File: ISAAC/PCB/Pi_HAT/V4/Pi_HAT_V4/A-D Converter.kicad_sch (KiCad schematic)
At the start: 1 part, among them U2 MCP3008-I/SL

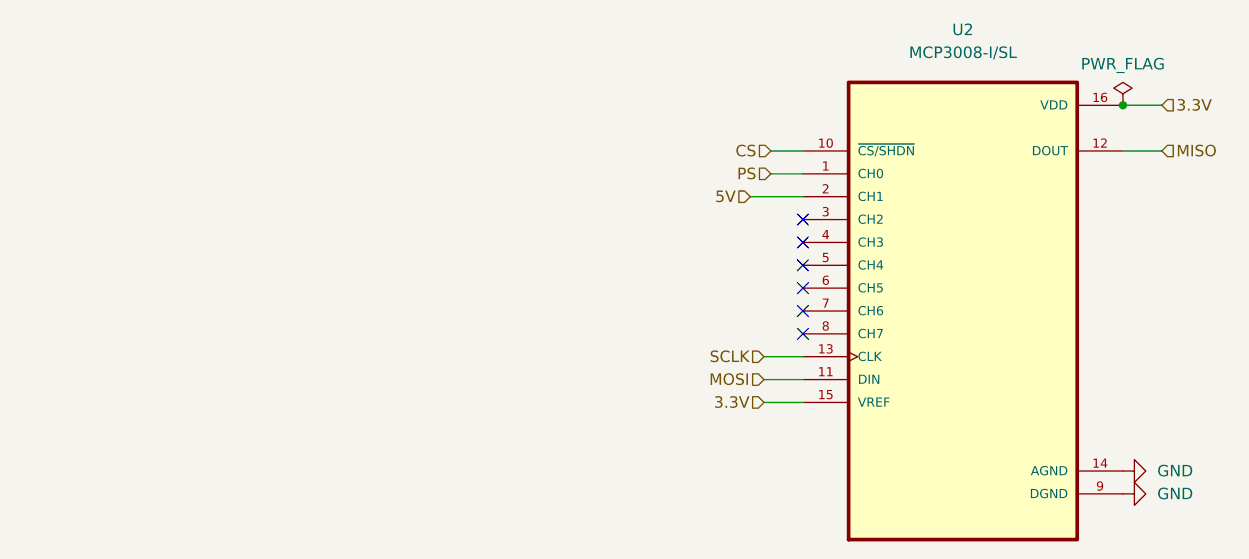
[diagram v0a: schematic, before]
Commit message: Updated
Started SPARK grant and updated controller and PCB
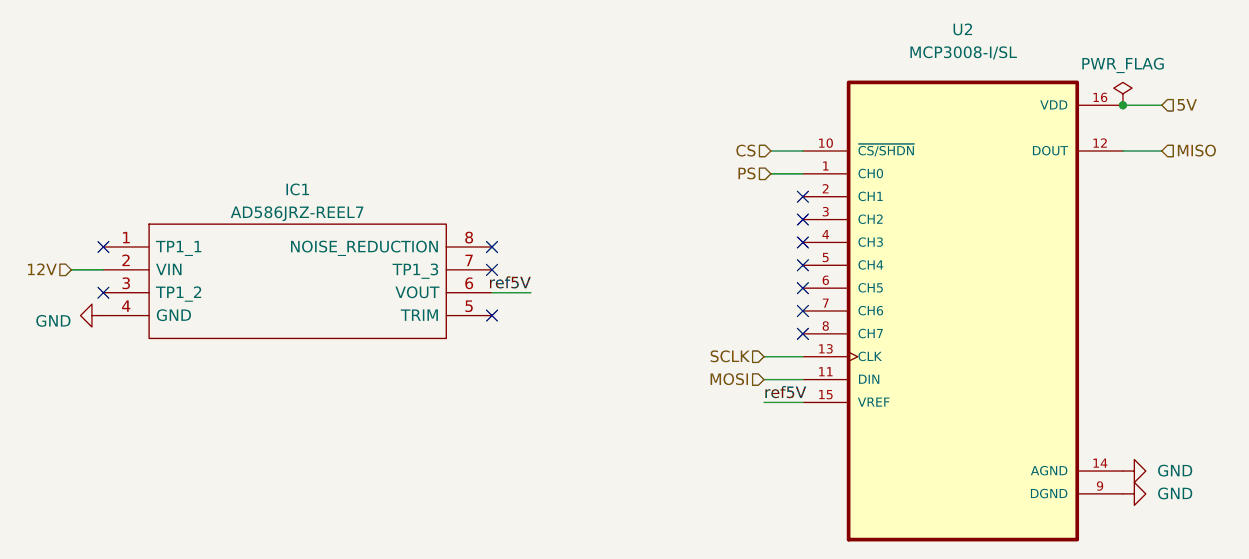
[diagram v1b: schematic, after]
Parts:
- added IC1: AD586JRZ-REEL7, refV:SOIC127P600X175-8N, symbol AD586JRZ-REEL7:AD586JRZ-REEL7
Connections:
- net 5V: now also U2.16 (VDD); no longer U2.2 (CH1)
- net GND: now also IC1.4 (GND)
- net 3.3V renamed ref5V
- net ref5V: now also IC1.6 (VOUT); no longer U2.16 (VDD)
- new net 12V: IC1.2 (VIN)
- no-connect marks 6 -> 12
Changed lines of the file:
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@@
   (junction (at 161.29 68.072) (diameter 0) (color 0 0 0 0)
   )
+  (no_connect (at 48.006 88.9))
+  (no_connect (at 48.006 83.82))
   (no_connect (at 125.73 88.392))
   (no_connect (at 125.73 90.932))
   (no_connect (at 125.73 93.472))
+  (no_connect (at 91.186 86.36))
+  (no_connect (at 125.73 78.232))
   (no_connect (at 125.73 83.312))
   (no_connect (at 125.73 85.852))
   (no_connect (at 125.73 80.772))
-  (wire (pts (xy 119.888 78.232) (xy 125.73 78.232))
-    (stroke (width 0) (type default))
-  )
+  (no_connect (at 91.186 91.44))
+  (no_connect (at 91.186 83.82))
   (wire (pts (xy 161.29 73.152) (xy 165.608 73.152))
     (stroke (width 0) (type default))
@@
     (stroke (width 0) (type default))
   )
+  (wire (pts (xy 44.45 86.36) (xy 48.006 86.36))
+    (stroke (width 0) (type default))
+  )
+  (wire (pts (xy 91.186 88.9) (xy 95.504 88.9))
+    (stroke (width 0) (type default))
+  )
   (wire (pts (xy 121.412 96.012) (xy 125.73 96.012))
     (stroke (width 0) (type default))
@@
     (stroke (width 0) (type default))
   )
-  (hierarchical_label "3.3V" (shape input) (at 121.412 101.092 180) (fields_autoplaced)
-    (effects (font (size 1.27 1.27)) (justify right))
+  (label "ref5V" (at 95.504 88.9 180) (fields_autoplaced)
+    (effects (font (size 1.27 1.27)) (justify right bottom))
   )
-  (hierarchical_label "3.3V" (shape input) (at 165.608 68.072 0) (fields_autoplaced)
-    (effects (font (size 1.27 1.27)) (justify left))
+  (label "ref5V" (at 121.412 101.092 0) (fields_autoplaced)
+    (effects (font (size 1.27 1.27)) (justify left bottom))
   )
   (hierarchical_label "SCLK" (shape input) (at 121.412 96.012 180) (fields_autoplaced)
@@
     (effects (font (size 1.27 1.27)) (justify left))
   )
-  (hierarchical_label "5V" (shape input) (at 119.888 78.232 180) (fields_autoplaced)
+  (hierarchical_label "12V" (shape input) (at 44.45 86.36 180) (fields_autoplaced)
     (effects (font (size 1.27 1.27)) (justify right))
+  )
+  (hierarchical_label "5V" (shape input) (at 165.608 68.072 0) (fields_autoplaced)
+    (effects (font (size 1.27 1.27)) (justify left))
   )
   (hierarchical_label "MOSI" (shape input) (at 121.412 98.552 180) (fields_autoplaced)
@@
   (hierarchical_label "PS" (shape input) (at 122.174 75.692 180) (fields_autoplaced)
     (effects (font (size 1.27 1.27)) (justify right))
+  )
+  (symbol (lib_id "AD586JRZ-REEL7:AD586JRZ-REEL7") (at 48.006 83.82 0) (unit 1)
+    (in_bom yes) (on_board yes) (dnp no) (fields_autoplaced)
+    (property "Reference" "IC1" (at 69.596 77.47 0)
+      (effects (font (size 1.27 1.27)))
+    )
+    (property "Value" "AD586JRZ-REEL7" (at 69.596 80.01 0)
+      (effects (font (size 1.27 1.27)))
+    )
+    (property "Footprint" "refV:SOIC127P600X175-8N" (at 87.376 81.28 0)
+      (effects (font (size 1.27 1.27)) (justify left) hide)
+    )
+    (property "Datasheet" "https://www.analog.com/media/en/technical-documentation/data-sheets/AD586.pdf" (at 87.376 83.82 0)
+      (effects (font (size 1.27 1.27)) (justify left) hide)
+    )
+    (property "Description" "Voltage References IC, MONO HI PREC .5V REF IC" (at 87.376 86.36 0)
+      (effects (font (size 1.27 1.27)) (justify left) hide)
+    )
+    (property "Height" "1.75" (at 87.376 88.9 0)
+      (effects (font (size 1.27 1.27)) (justify left) hide)
+    )
+    (property "Mouser Part Number" "584-AD586JRZ-R7" (at 87.376 91.44 0)
+      (effects (font (size 1.27 1.27)) (justify left) hide)
+    )
+    (property "Mouser Price/Stock" "https://www.mouser.co.uk/ProductDetail/Analog-Devices/AD586JRZ-REEL7?qs=NmRFExCfTkEQ7ye4ZY8tAg%3D%3D" (at 87.376 93.98 0)
+      (effects (font (size 1.27 1.27)) (justify left) hide)
+    )
+    (property "Manufacturer_Name" "Analog Devices" (at 87.376 96.52 0)
+      (effects (font (size 1.27 1.27)) (justify left) hide)
+    )
+    (property "Manufacturer_Part_Number" "AD586JRZ-REEL7" (at 87.376 99.06 0)
+      (effects (font (size 1.27 1.27)) (justify left) hide)
+    )
+    (pin "1")
+    (pin "2")
+    (pin "3")
+    (pin "4")
+    (pin "5")
+    (pin "6")
+    (pin "7")
+    (pin "8")
+    (instances
+      (project "Pi_HAT_V4"
+        (path "/e63e39d7-6ac0-4ffd-8aa3-1841a4541b55/048aae1f-d538-461c-a17b-6a2498319945"
+          (reference "IC1") (unit 1)
+        )
+      )
+    )
   )
   (symbol (lib_id "power:GND") (at 161.29 111.252 90) (unit 1)
@@
         )
       )
+    )
+  )
+  (symbol (lib_name "GND_1") (lib_id "power:GND") (at 48.006 91.44 270) (unit 1)
+    (in_bom yes) (on_board yes) (dnp no) (fields_autoplaced)
+    (property "Reference" "#PWR01" (at 41.656 91.44 0)
+      (effects (font (size 1.27 1.27)) hide)
+    )
+    (property "Value" "GND" (at 44.45 92.075 90)
+      (effects (font (size 1.27 1.27)) (justify right))
+    )
+    (property "Footprint" "" (at 48.006 91.44 0)
+      (effects (font (size 1.27 1.27)) hide)
+    )
+    (property "Datasheet" "" (at 48.006 91.44 0)
+      (effects (font (size 1.27 1.27)) hide)
+    )
+    (pin "1")
+    (instances
+      (project "Pi_HAT_V4"
+        (path "/e63e39d7-6ac0-4ffd-8aa3-1841a4541b55/048aae1f-d538-461c-a17b-6a2498319945"
+          (reference "#PWR01") (unit 1)
+        )
+      )
